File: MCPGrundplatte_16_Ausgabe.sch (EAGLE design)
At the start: 36 parts, among them IC1 ULN2803, IC2 74HC14N, IC3 74HC14N, X1GPA0-7 MKDSN1,5/9-5,08, X2 MKDSN1,5/2-5,08, X2GPB0-7 MKDSN1,5/9-5,08

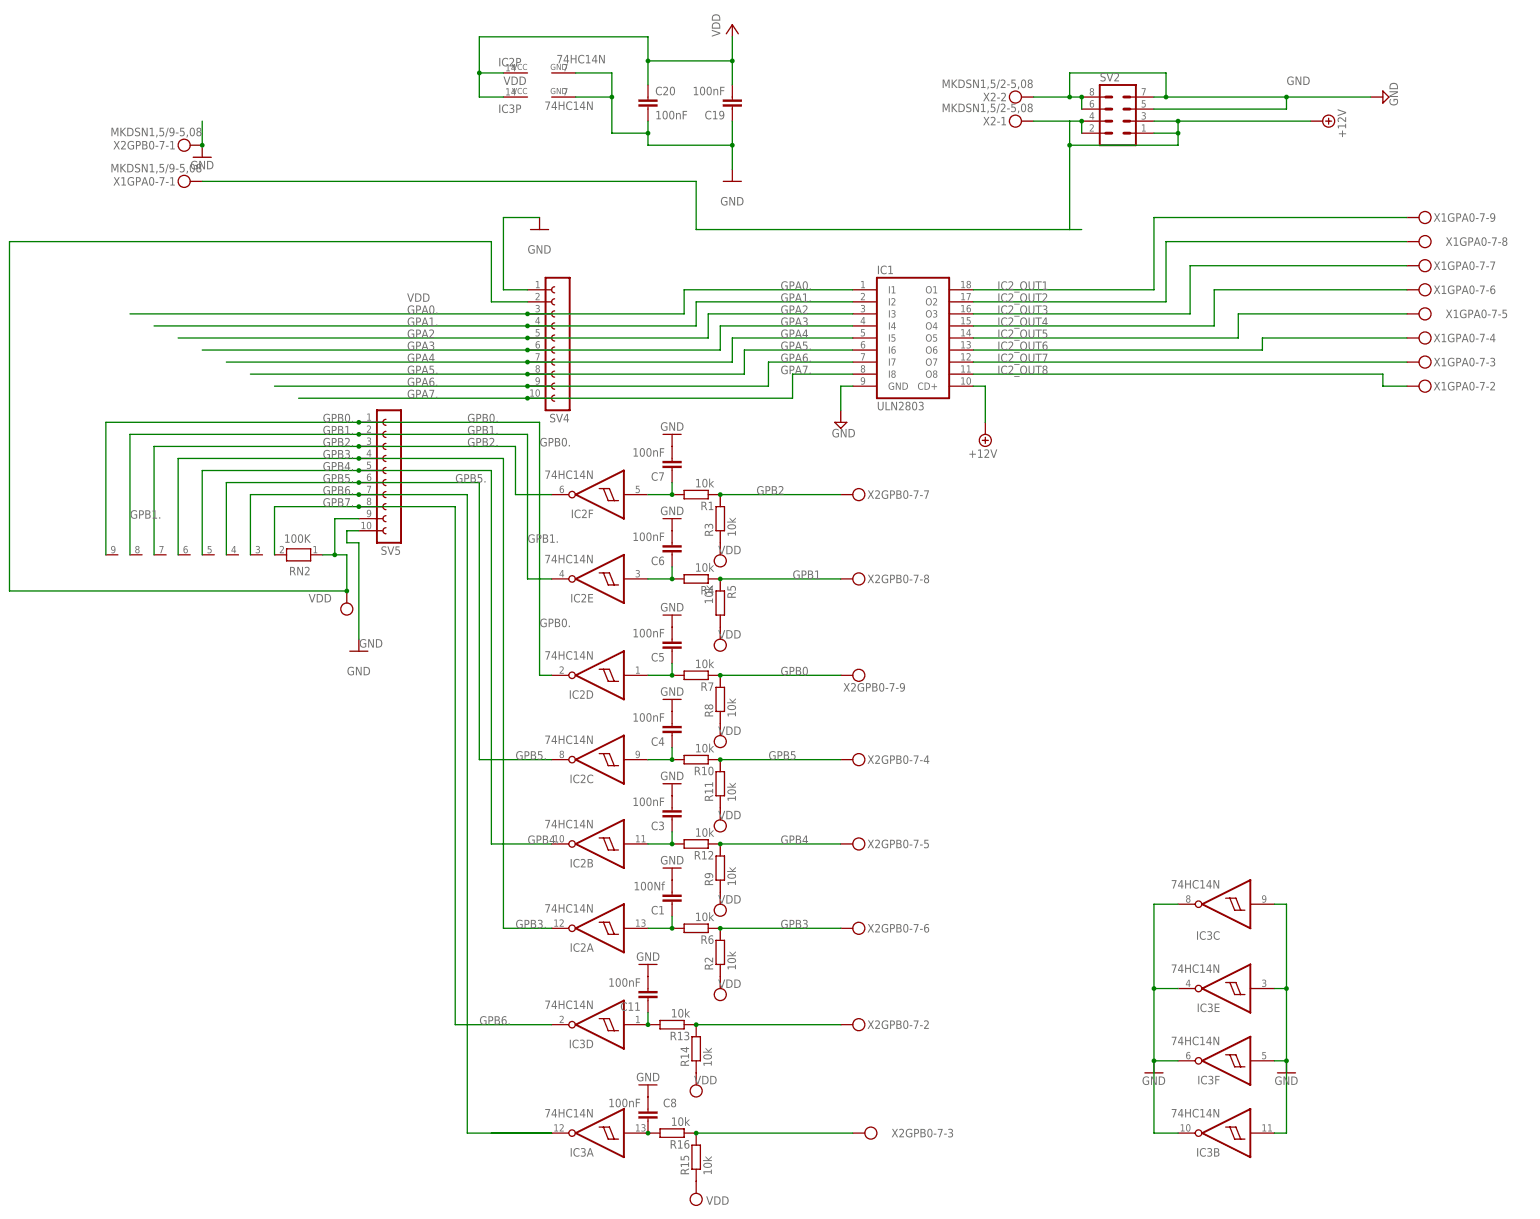
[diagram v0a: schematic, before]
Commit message: Neuen 16 Fach Output und 8In8Out hinzugefügt
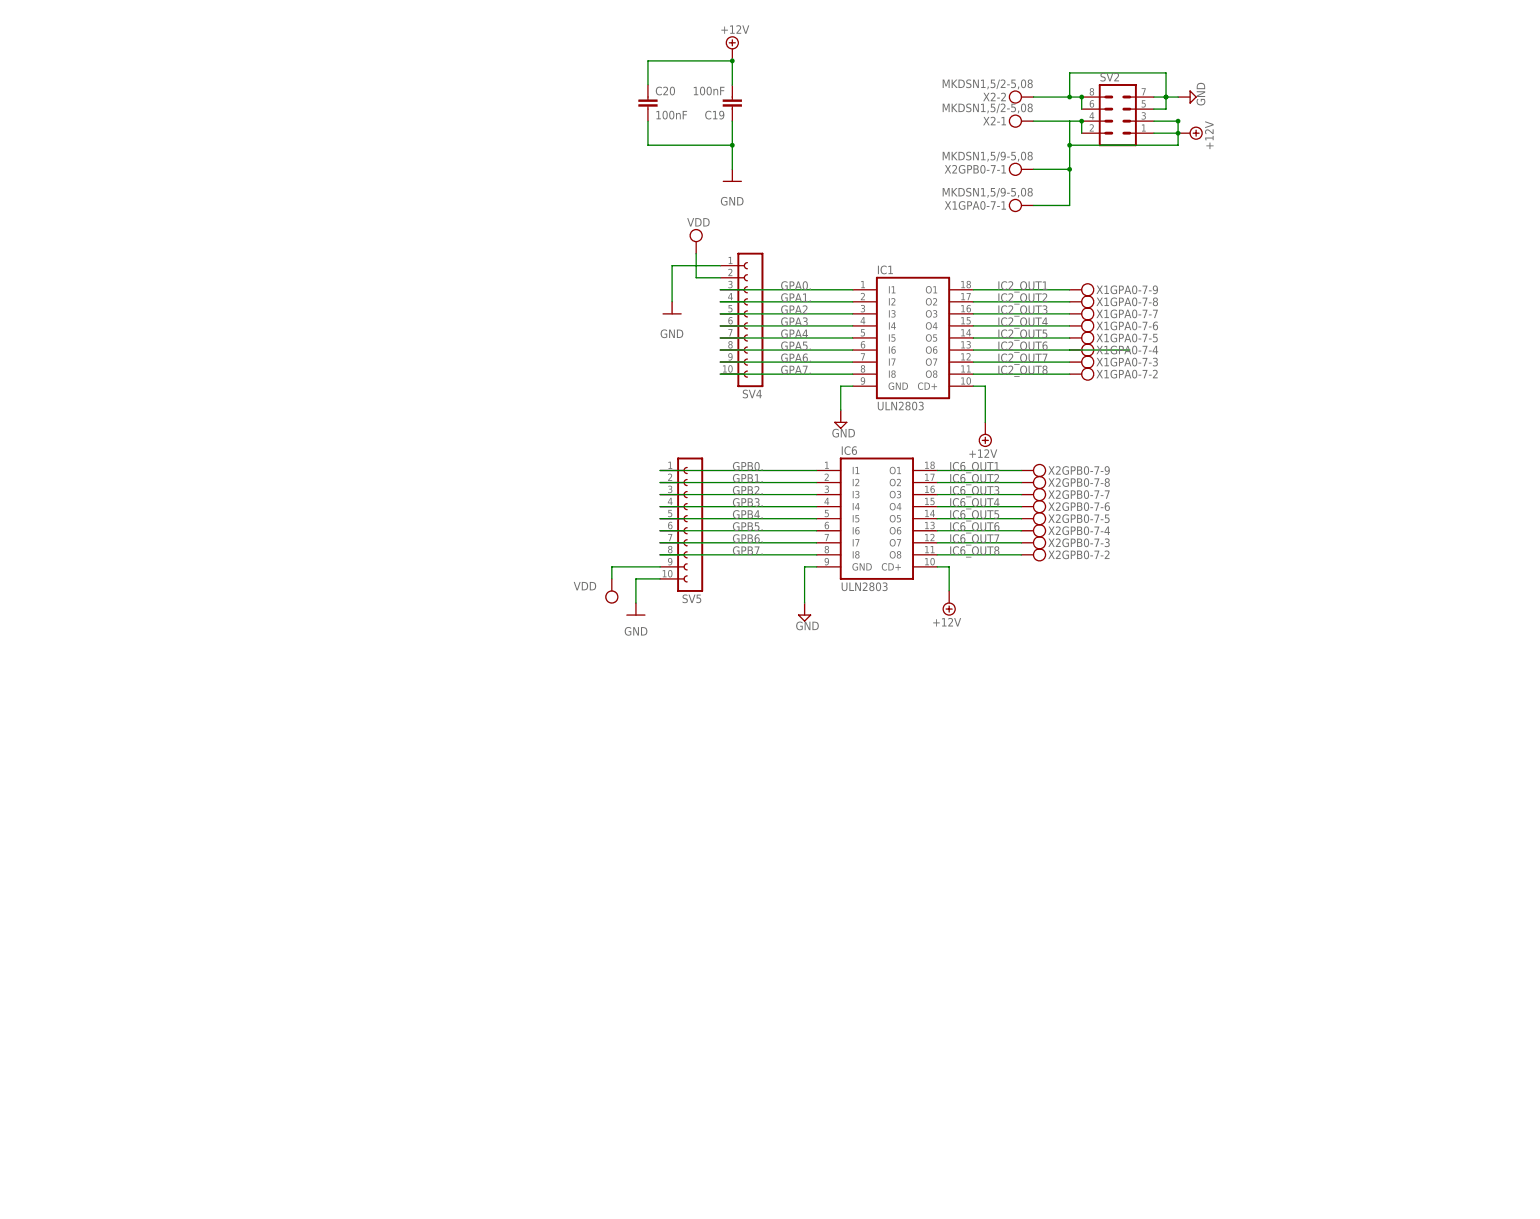
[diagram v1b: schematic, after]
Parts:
- removed C1: 100Nf, rcl:C-EU025-024X044
- removed C11, C3, C4, C5, C6, C7, C8: 100nF, rcl:C-EU025-024X044
- removed IC2, IC3: 74HC14N, 74xx-eu:74HC14N
- removed R1, R10, R11, R12, R13, R14, R15, R16, R2, R3, R4, R5, R6, R7, R8, R9: 10k, rcl:R-EU_0207/10
- removed RN2: 100K, resistor-net:RN08
- added IC6: ULN2803, uln-udn:ULN2803A
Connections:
- removed net GPB0: R7.1, R8.2, X2GPB0-7-9.KL
- removed net GPB1: R4.1, R5.1, X2GPB0-7-8.KL
- removed net GPB2: R1.1, R3.2, X2GPB0-7-7.KL
- removed net GPB3: R2.2, R6.1, X2GPB0-7-6.KL
- removed net GPB4: R12.1, R9.2, X2GPB0-7-5.KL
- removed net GPB5: R10.1, R11.2, X2GPB0-7-4.KL
- removed net GPB6: R15.2, R16.1, X2GPB0-7-3.KL
- removed net GPB7: R13.1, R14.2, X2GPB0-7-2.KL
- removed net N$11: C11.1, IC3D.I, R13.2
- removed net N$2: C7.1, IC2F.I, R1.2
- removed net N$4: C1.1, IC2A.I, R6.2
- removed net N$5: C6.1, IC2E.I, R4.2
- removed net N$6: C5.1, IC2D.I, R7.2
- removed net N$7: C4.1, IC2C.I, R10.2
- removed net N$8: C3.1, IC2B.I, R12.2
- removed net N$9: C8.1, IC3A.I, R16.2
- new net IC6_OUT1: IC6.O1, X2GPB0-7-9.KL
- new net IC6_OUT2: IC6.O2, X2GPB0-7-8.KL
- new net IC6_OUT3: IC6.O3, X2GPB0-7-7.KL
- new net IC6_OUT4: IC6.O4, X2GPB0-7-6.KL
- new net IC6_OUT5: IC6.O5, X2GPB0-7-5.KL
- new net IC6_OUT6: IC6.O6, X2GPB0-7-4.KL
- new net IC6_OUT7: IC6.O7, X2GPB0-7-3.KL
- new net IC6_OUT8: IC6.O8, X2GPB0-7-2.KL
- net +12V: now also C19.2, C20.1, IC6.CD+, X2GPB0-7-1.KL
- net GND: now also IC6.GND; no longer C1.2, C11.2, C3.2, C4.2, C5.2, C6.2, C7.2, C8.2, IC2P.GND, IC3B.I, IC3B.O, IC3C.I, IC3C.O, IC3E.I, IC3E.O, IC3F.I, IC3F.O, IC3P.GND, X2GPB0-7-1.KL
- net GPB0.: now also IC6.I1; no longer IC2D.O, RN2.9
- net GPB1.: now also IC6.I2; no longer IC2E.O, RN2.8
- net GPB2.: now also IC6.I3; no longer IC2F.O, RN2.7
- net GPB3.: now also IC6.I4; no longer IC2A.O, RN2.6
- net GPB4.: now also IC6.I5; no longer IC2B.O, RN2.5
- net GPB5.: now also IC6.I6; no longer IC2C.O, RN2.4
- net GPB6.: now also IC6.I7; no longer IC3A.O, RN2.3
- net GPB7.: now also IC6.I8; no longer IC3D.O, RN2.2
- net VDD: no longer C19.2, C20.1, IC2P.VCC, IC3P.VCC, R11.1, R14.1, R15.1, R2.1, R3.1, R5.2, R8.1, R9.1, RN2.1
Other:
- moved on the sheet: SV4, SV5, X1GPA0-7-1, X1GPA0-7-2, X1GPA0-7-3, X1GPA0-7-4, X1GPA0-7-5, X1GPA0-7-6, X1GPA0-7-7, X1GPA0-7-8, X1GPA0-7-9, X2GPB0-7-1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
